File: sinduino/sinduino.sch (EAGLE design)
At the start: 22 parts, among them IC1 IC_UC_ATMEGA32U4-TQFP44, Q1 16000, X1 MINI-USB-32005-301

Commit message: proceed connecting
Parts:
- added LED4: yellow, led:LED3MM
- added R6: 680, rcl:R-EU_R1206
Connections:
- new net D0: IC1.PD2, JP2.13
- new net D1: IC1.PD3, JP2.14
- new net D12: IC1.PD6, JP2.16
- new net D2: IC1.PD1, JP2.12
- new net D4: IC1.PD4, JP2.15
- new net D6: IC1.PD7, JP2.17
- new net N$11: LED4.C, R6.2
- new net N$2: IC1.PD5, R6.1
- net VCC: now also LED4.A
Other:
- moved on the sheet: JP2
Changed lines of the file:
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@@
 <part name="P+5" library="supply1" deviceset="VCC" device=""/>
 <part name="GND10" library="supply1" deviceset="GND" device=""/>
+<part name="R6" library="rcl" deviceset="R-EU_" device="R1206" value="680"/>
+<part name="LED4" library="led" deviceset="LED" device="3MM" value="yellow"/>
+<part name="P+1" library="supply1" deviceset="VCC" device=""/>
 </parts>
 <sheets>
@@
 <instance part="JP1" gate="1" x="109.22" y="73.66" rot="R90"/>
 <instance part="P+4" gate="VCC" x="119.38" y="96.52"/>
-<instance part="JP2" gate="G$1" x="53.34" y="111.76" rot="R90"/>
+<instance part="JP2" gate="G$1" x="53.34" y="114.3" rot="R90"/>
 <instance part="JP3" gate="G$1" x="83.82" y="7.62" rot="R270"/>
-<instance part="P+5" gate="VCC" x="25.4" y="109.22"/>
+<instance part="P+5" gate="VCC" x="25.4" y="111.76"/>
 <instance part="GND10" gate="1" x="55.88" y="-5.08"/>
+<instance part="R6" gate="G$1" x="88.9" y="91.44"/>
+<instance part="LED4" gate="G$1" x="96.52" y="99.06"/>
+<instance part="P+1" gate="VCC" x="96.52" y="111.76"/>
 </instances>
 <busses>
@@
 <segment>
 <pinref part="JP2" gate="G$1" pin="1"/>
-<wire x1="35.56" y1="109.22" x2="35.56" y2="96.52" width="0.1524" layer="91"/>
+<wire x1="35.56" y1="111.76" x2="35.56" y2="99.06" width="0.1524" layer="91"/>
 <pinref part="JP2" gate="G$1" pin="4"/>
-<wire x1="43.18" y1="109.22" x2="43.18" y2="96.52" width="0.1524" layer="91"/>
-<wire x1="43.18" y1="96.52" x2="40.64" y2="96.52" width="0.1524" layer="91"/>
-<wire x1="40.64" y1="96.52" x2="38.1" y2="96.52" width="0.1524" layer="91"/>
-<wire x1="38.1" y1="96.52" x2="35.56" y2="96.52" width="0.1524" layer="91"/>
-<wire x1="35.56" y1="96.52" x2="25.4" y2="96.52" width="0.1524" layer="91"/>
-<wire x1="25.4" y1="96.52" x2="25.4" y2="106.68" width="0.1524" layer="91"/>
-<junction x="35.56" y="96.52"/>
+<wire x1="43.18" y1="111.76" x2="43.18" y2="99.06" width="0.1524" layer="91"/>
+<wire x1="43.18" y1="99.06" x2="40.64" y2="99.06" width="0.1524" layer="91"/>
+<wire x1="40.64" y1="99.06" x2="38.1" y2="99.06" width="0.1524" layer="91"/>
+<wire x1="38.1" y1="99.06" x2="35.56" y2="99.06" width="0.1524" layer="91"/>
+<wire x1="35.56" y1="99.06" x2="25.4" y2="99.06" width="0.1524" layer="91"/>
+<wire x1="25.4" y1="99.06" x2="25.4" y2="109.22" width="0.1524" layer="91"/>
+<junction x="35.56" y="99.06"/>
 <pinref part="JP2" gate="G$1" pin="2"/>
-<wire x1="38.1" y1="109.22" x2="38.1" y2="96.52" width="0.1524" layer="91"/>
-<junction x="38.1" y="96.52"/>
+<wire x1="38.1" y1="111.76" x2="38.1" y2="99.06" width="0.1524" layer="91"/>
+<junction x="38.1" y="99.06"/>
 <pinref part="JP2" gate="G$1" pin="3"/>
-<wire x1="40.64" y1="109.22" x2="40.64" y2="96.52" width="0.1524" layer="91"/>
-<junction x="40.64" y="96.52"/>
+<wire x1="40.64" y1="111.76" x2="40.64" y2="99.06" width="0.1524" layer="91"/>
+<junction x="40.64" y="99.06"/>
 <pinref part="P+5" gate="VCC" pin="VCC"/>
-<wire x1="25.4" y1="96.52" x2="25.4" y2="88.9" width="0.1524" layer="91"/>
+<wire x1="25.4" y1="99.06" x2="25.4" y2="88.9" width="0.1524" layer="91"/>
 <pinref part="R3" gate="G$1" pin="2"/>
 <wire x1="30.48" y1="83.82" x2="30.48" y2="88.9" width="0.1524" layer="91"/>
@@
 <wire x1="30.48" y1="88.9" x2="40.64" y2="88.9" width="0.1524" layer="91"/>
 <junction x="30.48" y="88.9"/>
-<junction x="25.4" y="96.52"/>
+<junction x="25.4" y="99.06"/>
+</segment>
+<segment>
+<pinref part="LED4" gate="G$1" pin="A"/>
+<pinref part="P+1" gate="VCC" pin="VCC"/>
+<wire x1="96.52" y1="101.6" x2="96.52" y2="109.22" width="0.1524" layer="91"/>
 </segment>
 </net>
@@
 <segment>
 <pinref part="JP2" gate="G$1" pin="10"/>
-<wire x1="58.42" y1="109.22" x2="58.42" y2="96.52" width="0.1524" layer="91"/>
-<label x="58.42" y="96.52" size="1.778" layer="95" rot="R90"/>
+<wire x1="58.42" y1="111.76" x2="58.42" y2="99.06" width="0.1524" layer="91"/>
+<label x="58.42" y="99.06" size="1.778" layer="95" rot="R90"/>
 </segment>
 </net>
@@
 <segment>
 <pinref part="JP2" gate="G$1" pin="5"/>
-<wire x1="45.72" y1="109.22" x2="45.72" y2="96.52" width="0.1524" layer="91"/>
-<label x="45.72" y="96.52" size="1.778" layer="95" rot="R90"/>
+<wire x1="45.72" y1="111.76" x2="45.72" y2="99.06" width="0.1524" layer="91"/>
+<label x="45.72" y="99.06" size="1.778" layer="95" rot="R90"/>
 </segment>
 </net>
@@
 <segment>
 <pinref part="JP2" gate="G$1" pin="6"/>
-<wire x1="48.26" y1="109.22" x2="48.26" y2="96.52" width="0.1524" layer="91"/>
-<label x="48.26" y="96.52" size="1.778" layer="95" rot="R90"/>
+<wire x1="48.26" y1="111.76" x2="48.26" y2="99.06" width="0.1524" layer="91"/>
+<label x="48.26" y="99.06" size="1.778" layer="95" rot="R90"/>
 </segment>
 <segment>
@@
 <segment>
 <pinref part="JP2" gate="G$1" pin="7"/>
-<wire x1="50.8" y1="109.22" x2="50.8" y2="96.52" width="0.1524" layer="91"/>
-<label x="50.8" y="96.52" size="1.778" layer="95" rot="R90"/>
+<wire x1="50.8" y1="111.76" x2="50.8" y2="99.06" width="0.1524" layer="91"/>
+<label x="50.8" y="99.06" size="1.778" layer="95" rot="R90"/>
 </segment>
 <segment>
@@
 <segment>
 <pinref part="JP2" gate="G$1" pin="8"/>
-<wire x1="53.34" y1="109.22" x2="53.34" y2="96.52" width="0.1524" layer="91"/>
-<label x="53.34" y="96.52" size="1.778" layer="95" rot="R90"/>
+<wire x1="53.34" y1="111.76" x2="53.34" y2="99.06" width="0.1524" layer="91"/>
+<label x="53.34" y="99.06" size="1.778" layer="95" rot="R90"/>
 </segment>
 <segment>
@@
 <segment>
 <pinref part="JP2" gate="G$1" pin="9"/>
-<wire x1="55.88" y1="109.22" x2="55.88" y2="96.52" width="0.1524" layer="91"/>
-<label x="55.88" y="96.52" size="1.778" layer="95" rot="R90"/>
+<wire x1="55.88" y1="111.76" x2="55.88" y2="99.06" width="0.1524" layer="91"/>
+<label x="55.88" y="99.06" size="1.778" layer="95" rot="R90"/>
 </segment>
 </net>
@@
 <segment>
 <pinref part="JP2" gate="G$1" pin="11"/>
-<wire x1="60.96" y1="109.22" x2="60.96" y2="88.9" width="0.1524" layer="91"/>
+<wire x1="60.96" y1="111.76" x2="60.96" y2="88.9" width="0.1524" layer="91"/>
 <pinref part="IC1" gate="IC" pin="PD0"/>
-<label x="60.96" y="96.52" size="1.778" layer="95" rot="R90"/>
-</segment>
-</net>
+<label x="60.96" y="99.06" size="1.778" layer="95" rot="R90"/>
+</segment>
+</net>
+<net name="D2" class="0">
+<segment>
+<pinref part="JP2" gate="G$1" pin="12"/>
+<pinref part="IC1" gate="IC" pin="PD1"/>
+<wire x1="63.5" y1="111.76" x2="63.5" y2="88.9" width="0.1524" layer="91"/>
+<label x="63.5" y="99.06" size="1.778" layer="95" rot="R90"/>
+</segment>
+</net>
+<net name="D0" class="0">
+<segment>
+<pinref part="IC1" gate="IC" pin="PD2"/>
+<pinref part="JP2" gate="G$1" pin="13"/>
+<wire x1="66.04" y1="88.9" x2="66.04" y2="111.76" width="0.1524" layer="91"/>
+<label x="66.04" y="99.06" size="1.778" layer="95" rot="R90"/>
+</segment>
+</net>
+<net name="D1" class="0">
+<segment>
+<pinref part="IC1" gate="IC" pin="PD3"/>
+<pinref part="JP2" gate="G$1" pin="14"/>
+<wire x1="68.58" y1="88.9" x2="68.58" y2="111.76" width="0.1524" layer="91"/>
+<label x="68.58" y="99.06" size="1.778" layer="95" rot="R90"/>
+</segment>
+</net>
+<net name="D4" class="0">
+<segment>
+<pinref part="IC1" gate="IC" pin="PD4"/>
+<pinref part="JP2" gate="G$1" pin="15"/>
+<wire x1="71.12" y1="88.9" x2="71.12" y2="111.76" width="0.1524" layer="91"/>
+<label x="71.12" y="99.06" size="1.778" layer="95" rot="R90"/>
+</segment>
+</net>
+<net name="D12" class="0">
+<segment>
+<pinref part="IC1" gate="IC" pin="PD6"/>
+<wire x1="76.2" y1="88.9" x2="76.2" y2="93.98" width="0.1524" layer="91"/>
+<wire x1="76.2" y1="93.98" x2="73.66" y2="93.98" width="0.1524" layer="91"/>
+<pinref part="JP2" gate="G$1" pin="16"/>
+<wire x1="73.66" y1="93.98" x2="73.66" y2="111.76" width="0.1524" layer="91"/>
+<label x="73.66" y="99.06" size="1.778" layer="95" rot="R90"/>
+</segment>
+</net>
+<net name="D6" class="0">
+<segment>
+<pinref part="IC1" gate="IC" pin="PD7"/>
+<wire x1="78.74" y1="88.9" x2="78.74" y2="96.52" width="0.1524" layer="91"/>
+<wire x1="78.74" y1="96.52" x2="76.2" y2="96.52" width="0.1524" layer="91"/>
+<pinref part="JP2" gate="G$1" pin="17"/>
+<wire x1="76.2" y1="96.52" x2="76.2" y2="111.76" width="0.1524" layer="91"/>
+<label x="76.2" y="99.06" size="1.778" layer="95" rot="R90"/>
+</segment>
+</net>
+<net name="N$2" class="0">
+<segment>
+<pinref part="IC1" gate="IC" pin="PD5"/>
+<wire x1="73.66" y1="88.9" x2="73.66" y2="91.44" width="0.1524" layer="91"/>
+<pinref part="R6" gate="G$1" pin="1"/>
+<wire x1="73.66" y1="91.44" x2="83.82" y2="91.44" width="0.1524" layer="91"/>
+</segment>
+</net>
+<net name="N$11" class="0">
+<segment>
+<pinref part="R6" gate="G$1" pin="2"/>
+<wire x1="93.98" y1="91.44" x2="96.52" y2="91.44" width="0.1524" layer="91"/>
+<pinref part="LED4" gate="G$1" pin="C"/>
+<wire x1="96.52" y1="91.44" x2="96.52" y2="93.98" width="0.1524" layer="91"/>
+</segment>
+</net>

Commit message: almost connected everything
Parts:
- added IC2: TS2940CT5TV, n39:TS2940CT5TV
- added R5: 3k9, rcl:R-EU_R1206
- added U$3: RIACON_101_2, n39:RIACON_101_2
- C1: value 100u -> 470n; device rcl:CPOL-EUE2.5-6 -> rcl:C-EU025-025X050
- C2: value 100u -> 33u
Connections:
- new net A0: IC1.PF7, JP3.6
- new net A1: IC1.PF6, JP3.7
- new net A2: IC1.PF5, JP3.8
- new net A3: IC1.PF4, JP3.9
- new net A4: IC1.PF1, JP3.10
- new net A5: IC1.PF0, JP3.11
- new net AREF: C7.1, IC1.AREF, JP3.12
- new net D13: IC1.PC7, JP3.5
- new net D5: IC1.PC6, JP3.4
- new net D7: IC1.PE6, JP3.13
- new net HWB: IC1.PE2, R5.2
- new net N$12: IC1.PB5, JP3.2
- new net N$13: IC1.PB4, JP3.1
- new net N$15: C1.1, IC2.IN, U$3.2
- new net N$16: C2.+, IC2.OUT, JP1.3
- net GND: now also C1.2, C2.-, IC2.GND, R5.1, U$3.1
- net N$1: now also IC1.PB6, JP3.3; no longer C7.1, IC1.AREF
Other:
- moved on the sheet: C2, F1, JP1, JP3, R7, R8, X1

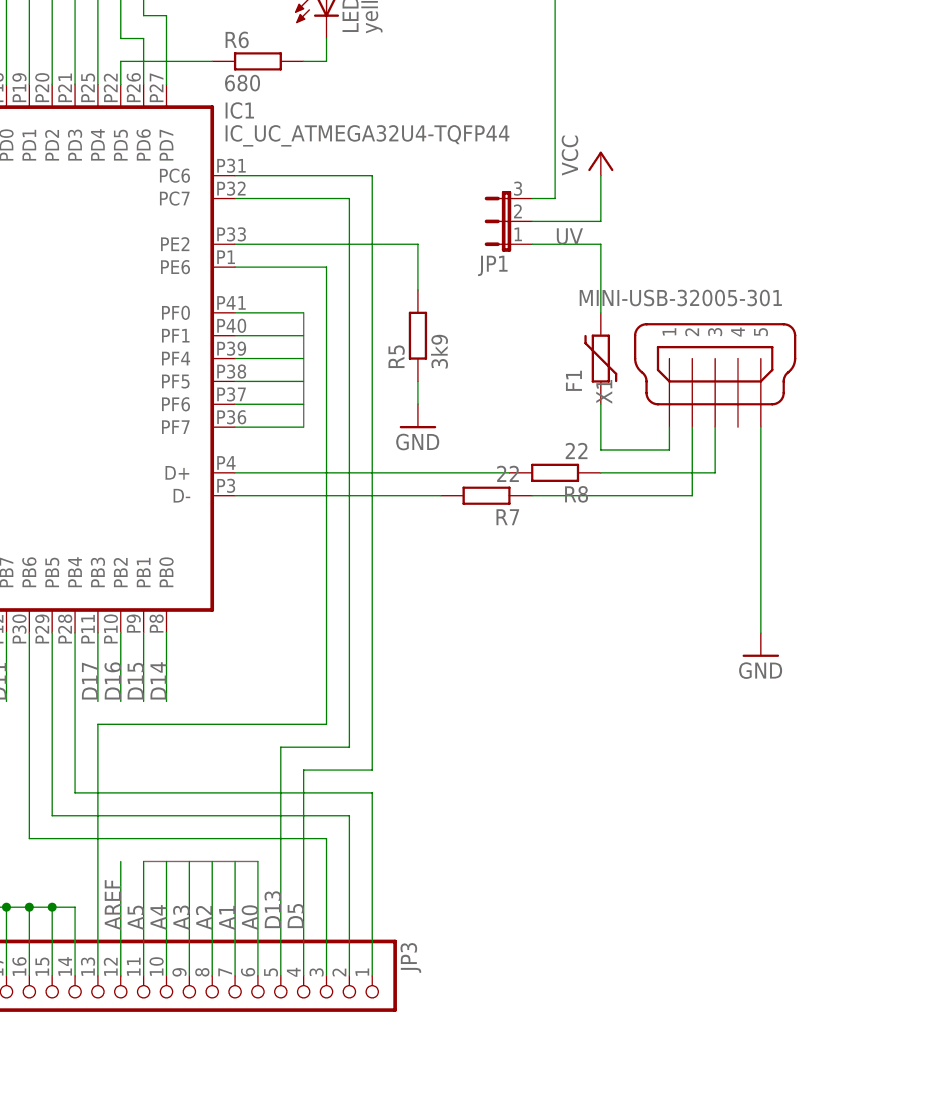
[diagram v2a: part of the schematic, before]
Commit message: complete schematic and start routing
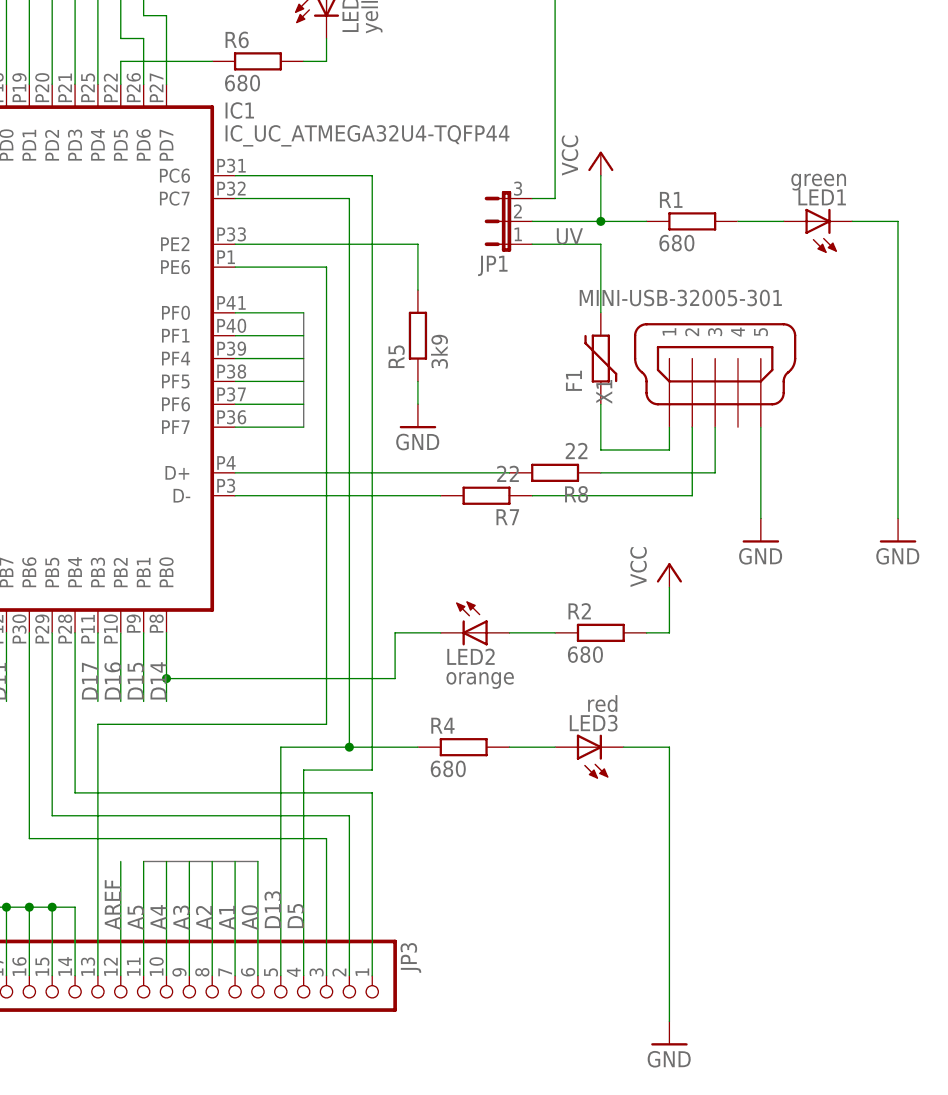
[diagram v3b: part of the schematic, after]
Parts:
- added LED1: green, led:LED3MM
- added LED2: orange, led:LED3MM
- added LED3: red, led:LED3MM
- added R1, R2, R4: 680, rcl:R-EU_R1206
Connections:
- new net N$14: LED1.A, R1.2
- new net N$17: LED2.A, R2.1
- new net N$18: LED3.A, R4.2
- net D13: now also R4.1
- net D14: now also LED2.C
- net GND: now also LED1.C, LED3.C
- net VCC: now also R1.1, R2.2

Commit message: switched one led with its resistor
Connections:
- net D13: now also LED3.A; no longer R4.1
- net GND: now also R4.2; no longer LED3.C
- net N$18: now also LED3.C, R4.1; no longer LED3.A, R4.2
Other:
- moved on the sheet: LED3, R4
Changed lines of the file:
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@@
 <instance part="LED2" gate="G$1" x="114.3" y="27.94" rot="R270"/>
 <instance part="GND14" gate="1" x="134.62" y="-17.78"/>
-<instance part="R4" gate="G$1" x="111.76" y="15.24"/>
-<instance part="LED3" gate="G$1" x="124.46" y="15.24" rot="R90"/>
+<instance part="R4" gate="G$1" x="127" y="15.24"/>
+<instance part="LED3" gate="G$1" x="111.76" y="15.24" rot="R90"/>
 <instance part="P+3" gate="VCC" x="134.62" y="35.56"/>
 </instances>
@@
 <segment>
 <pinref part="GND14" gate="1" pin="GND"/>
-<pinref part="LED3" gate="G$1" pin="C"/>
 <wire x1="134.62" y1="15.24" x2="134.62" y2="-15.24" width="0.1524" layer="91"/>
-<wire x1="129.54" y1="15.24" x2="134.62" y2="15.24" width="0.1524" layer="91"/>
+<pinref part="R4" gate="G$1" pin="2"/>
+<wire x1="132.08" y1="15.24" x2="134.62" y2="15.24" width="0.1524" layer="91"/>
 </segment>
 </net>
@@
 <wire x1="91.44" y1="15.24" x2="91.44" y2="-10.16" width="0.1524" layer="91"/>
 <label x="91.44" y="-5.08" size="1.778" layer="95" rot="R90"/>
-<pinref part="R4" gate="G$1" pin="1"/>
-<wire x1="99.06" y1="15.24" x2="106.68" y2="15.24" width="0.1524" layer="91"/>
+<pinref part="LED3" gate="G$1" pin="A"/>
+<wire x1="99.06" y1="15.24" x2="109.22" y2="15.24" width="0.1524" layer="91"/>
 <junction x="99.06" y="15.24"/>
 </segment>
@@
 </segment>
 </net>
-<net name="N$18" class="0">
-<segment>
-<pinref part="R4" gate="G$1" pin="2"/>
-<pinref part="LED3" gate="G$1" pin="A"/>
-<wire x1="116.84" y1="15.24" x2="121.92" y2="15.24" width="0.1524" layer="91"/>
-</segment>
-</net>
 <net name="N$17" class="0">
 <segment>
@@
 </segment>
 </net>
+<net name="N$18" class="0">
+<segment>
+<pinref part="LED3" gate="G$1" pin="C"/>
+<pinref part="R4" gate="G$1" pin="1"/>
+<wire x1="116.84" y1="15.24" x2="121.92" y2="15.24" width="0.1524" layer="91"/>
+</segment>
+</net>

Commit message: routed all the stuff around the xtal
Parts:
- C2: device rcl:CPOL-EUE2.5-6 -> rcl:CPOL-EUE2.5-5
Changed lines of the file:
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@@
 <grid distance="0.1" unitdist="inch" unit="inch" style="lines" multiple="1" display="no" altdistance="0.01" altunitdist="inch" altunit="inch"/>
 <layers>
-<layer number="1" name="Top" color="4" fill="1" visible="no" active="no"/>
-<layer number="16" name="Bottom" color="1" fill="1" visible="no" active="no"/>
-<layer number="17" name="Pads" color="2" fill="1" visible="no" active="no"/>
-<layer number="18" name="Vias" color="2" fill="1" visible="no" active="no"/>
-<layer number="19" name="Unrouted" color="6" fill="1" visible="no" active="no"/>
-<layer number="20" name="Dimension" color="15" fill="1" visible="no" active="no"/>
-<layer number="21" name="tPlace" color="7" fill="1" visible="no" active="no"/>
-<layer number="22" name="bPlace" color="7" fill="1" visible="no" active="no"/>
-<layer number="23" name="tOrigins" color="15" fill="1" visible="no" active="no"/>
-<layer number="24" name="bOrigins" color="15" fill="1" visible="no" active="no"/>
-<layer number="25" name="tNames" color="7" fill="1" visible="no" active="no"/>
-<layer number="26" name="bNames" color="7" fill="1" visible="no" active="no"/>
-<layer number="27" name="tValues" color="7" fill="1" visible="no" active="no"/>
-<layer number="28" name="bValues" color="7" fill="1" visible="no" active="no"/>
+<layer number="1" name="Top" color="4" fill="1" visible="yes" active="no"/>
+<layer number="16" name="Bottom" color="1" fill="1" visible="yes" active="no"/>
+<layer number="17" name="Pads" color="2" fill="1" visible="yes" active="no"/>
+<layer number="18" name="Vias" color="2" fill="1" visible="yes" active="no"/>
+<layer number="19" name="Unrouted" color="6" fill="1" visible="yes" active="no"/>
+<layer number="20" name="Dimension" color="15" fill="1" visible="yes" active="no"/>
+<layer number="21" name="tPlace" color="7" fill="1" visible="yes" active="no"/>
+<layer number="22" name="bPlace" color="7" fill="1" visible="yes" active="no"/>
+<layer number="23" name="tOrigins" color="15" fill="1" visible="yes" active="no"/>
+<layer number="24" name="bOrigins" color="15" fill="1" visible="yes" active="no"/>
+<layer number="25" name="tNames" color="7" fill="1" visible="yes" active="no"/>
+<layer number="26" name="bNames" color="7" fill="1" visible="yes" active="no"/>
+<layer number="27" name="tValues" color="7" fill="1" visible="yes" active="no"/>
+<layer number="28" name="bValues" color="7" fill="1" visible="yes" active="no"/>
 <layer number="29" name="tStop" color="7" fill="3" visible="no" active="no"/>
 <layer number="30" name="bStop" color="7" fill="6" visible="no" active="no"/>
@@
 <layer number="35" name="tGlue" color="7" fill="4" visible="no" active="no"/>
 <layer number="36" name="bGlue" color="7" fill="5" visible="no" active="no"/>
-<layer number="37" name="tTest" color="7" fill="1" visible="no" active="no"/>
-<layer number="38" name="bTest" color="7" fill="1" visible="no" active="no"/>
+<layer number="37" name="tTest" color="7" fill="1" visible="yes" active="no"/>
+<layer number="38" name="bTest" color="7" fill="1" visible="yes" active="no"/>
 <layer number="39" name="tKeepout" color="4" fill="11" visible="no" active="no"/>
 <layer number="40" name="bKeepout" color="1" fill="11" visible="no" active="no"/>
@@
 <layer number="44" name="Drills" color="7" fill="1" visible="no" active="no"/>
 <layer number="45" name="Holes" color="7" fill="1" visible="no" active="no"/>
-<layer number="46" name="Milling" color="3" fill="1" visible="no" active="no"/>
-<layer number="47" name="Measures" color="7" fill="1" visible="no" active="no"/>
-<layer number="48" name="Document" color="7" fill="1" visible="no" active="no"/>
-<layer number="49" name="Reference" color="7" fill="1" visible="no" active="no"/>
-<layer number="50" name="dxf" color="7" fill="1" visible="no" active="no"/>
-<layer number="51" name="wire" color="7" fill="1" visible="no" active="no"/>
-<layer number="52" name="bDocu" color="7" fill="1" visible="no" active="no"/>
-<layer number="53" name="tGND_GNDA" color="7" fill="1" visible="no" active="no"/>
-<layer number="54" name="bGND_GNDA" color="7" fill="1" visible="no" active="no"/>
-<layer number="56" name="wert" color="7" fill="1" visible="no" active="no"/>
+<layer number="46" name="Milling" color="3" fill="1" visible="yes" active="no"/>
+<layer number="47" name="Measures" color="7" fill="1" visible="yes" active="no"/>
+<layer number="48" name="Document" color="7" fill="1" visible="yes" active="no"/>
+<layer number="49" name="Reference" color="7" fill="1" visible="yes" active="no"/>
+<layer number="50" name="dxf" color="7" fill="1" visible="yes" active="no"/>
+<layer number="51" name="wire" color="7" fill="1" visible="yes" active="no"/>
+<layer number="52" name="bDocu" color="7" fill="1" visible="yes" active="no"/>
+<layer number="53" name="tGND_GNDA" color="7" fill="1" visible="yes" active="no"/>
+<layer number="54" name="bGND_GNDA" color="7" fill="1" visible="yes" active="no"/>
+<layer number="56" name="wert" color="7" fill="1" visible="yes" active="no"/>
 <layer number="91" name="Nets" color="2" fill="1" visible="yes" active="yes"/>
 <layer number="92" name="Busses" color="1" fill="1" visible="yes" active="yes"/>
@@
 <part name="IC1" library="dp_devices" deviceset="IC_UC_ATMEGA32U4" device="-TQFP44"/>
 <part name="C1" library="rcl" deviceset="C-EU" device="025-025X050" value="470n"/>
-<part name="C2" library="rcl" deviceset="CPOL-EU" device="E2.5-6" value="33u"/>
+<part name="C2" library="rcl" deviceset="CPOL-EU" device="E2.5-5" value="33u"/>
 <part name="C3" library="rcl" deviceset="C-EU" device="C1206" value="100n"/>
 <part name="C4" library="rcl" deviceset="C-EU" device="C1206" value="100n"/>
